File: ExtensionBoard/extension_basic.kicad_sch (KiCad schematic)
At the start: 11 parts, among them U1 KH-2.54FH-1X15P-H8.5, U1 Unidirectional 5.5V 6V SOT-14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, U2 C193852, U2 PM2.54-2*15, U3 KH-2.54PH180-3X15P-L11.5

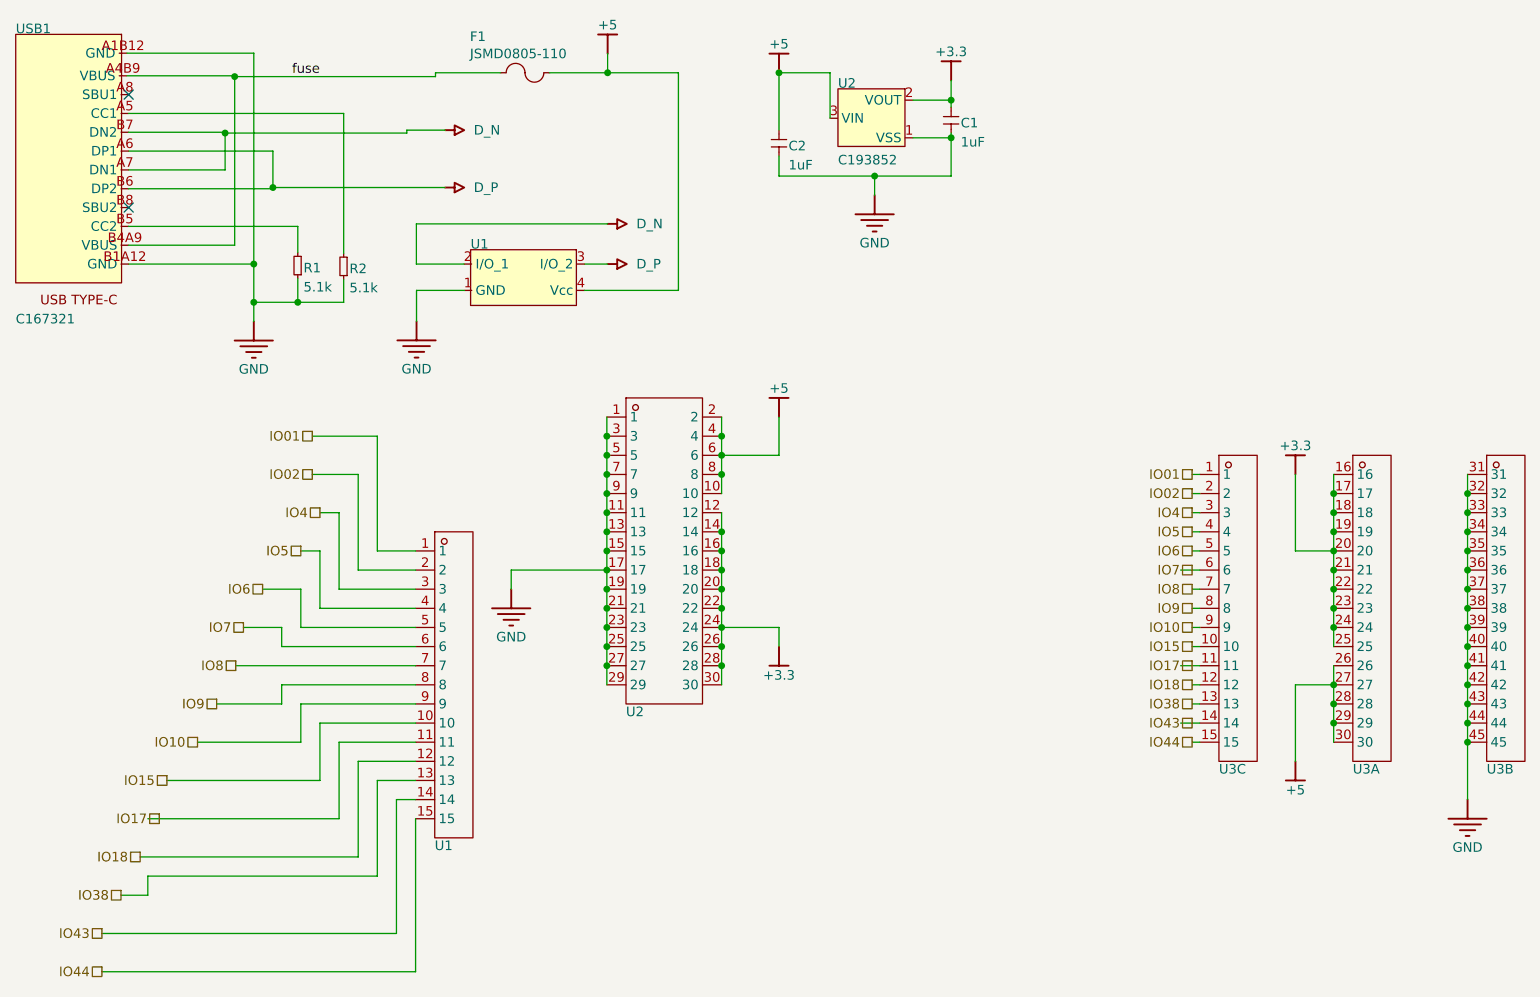
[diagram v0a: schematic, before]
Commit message: extension board imported
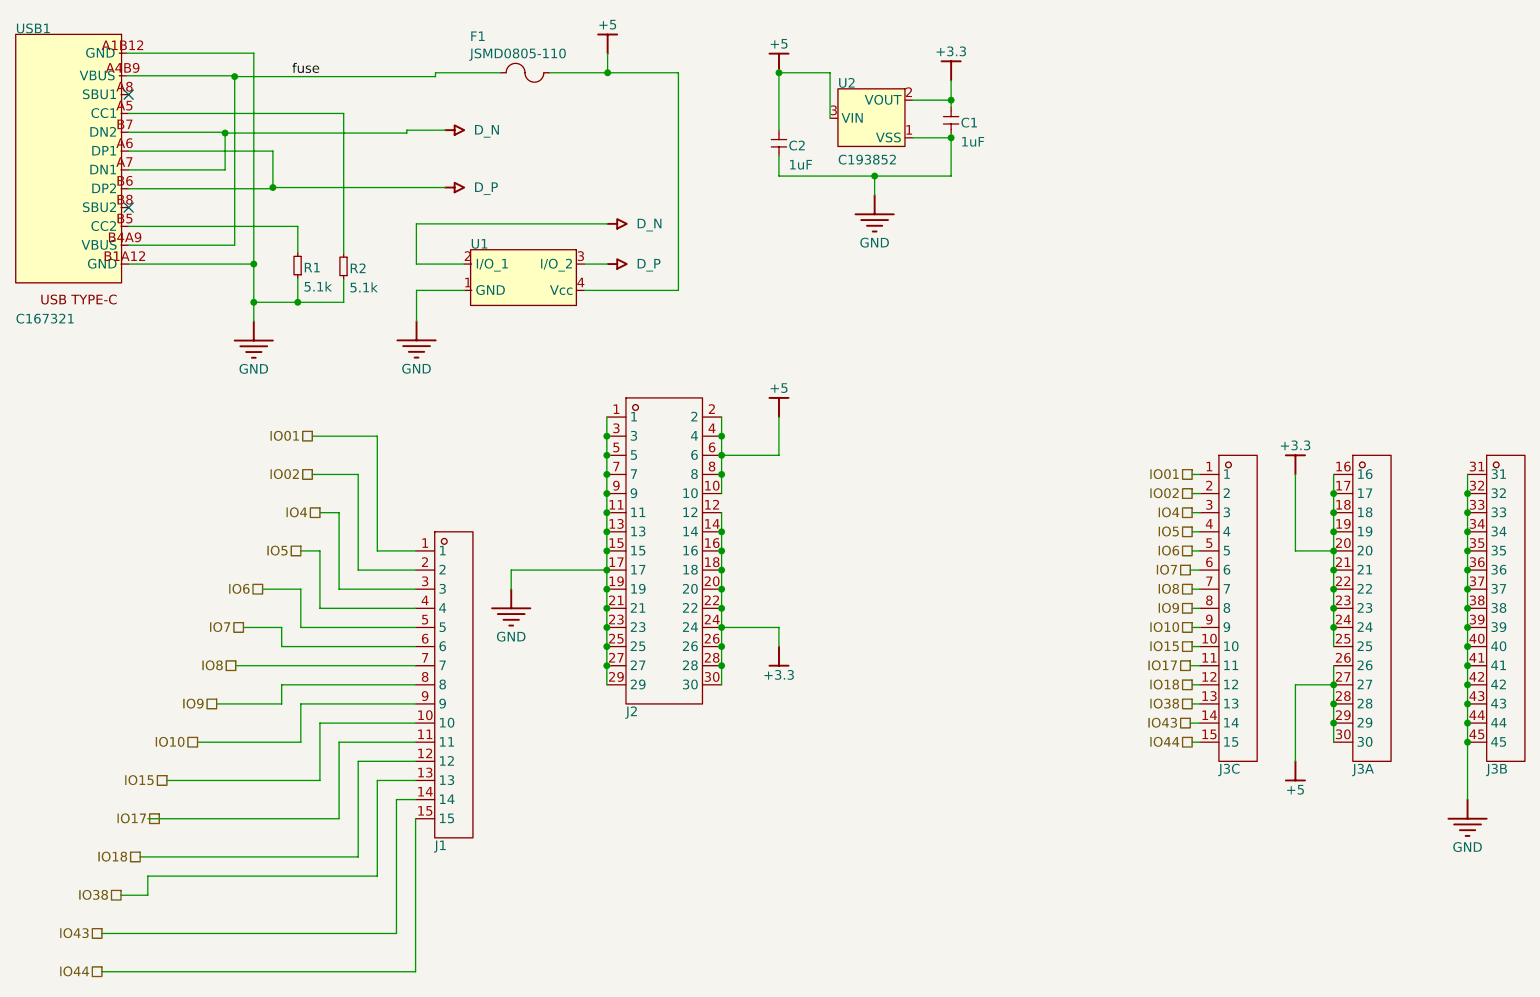
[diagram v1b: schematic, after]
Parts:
- removed U1: KH-2.54FH-1X15P-H8.5, HDR-TH_15P-P2.54-V-F, symbol KH-2.54FH-1X15P-H8.51_KH-2.54FH-1X15P-H8.5:root_0_KH-2.54FH-1X15P-H8.5_KH-2.54F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
- removed U2: PM2.54-2*15, HDR-TH_30P-P2.54-V-F-R2-C15-S2.54, symbol PM2.54-2_151_PM2.54-2_15:root_0_PM2.54-2*15_PM2.54-2_151_PM2.54-2_15.SCHLIB
- removed U3: KH-2.54PH180-3X15P-L11.5, HDR-TH_15P-P2.54-V-M-R3-C15-S2.54, symbol KH-2.54PH180-3X15P-L11.51_KH-2.54PH180-3X15P-L11.5:root_0_KH-2.54PH180-3X15P-L1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
- added J1: KH-2.54FH-1X15P-H8.5, FableFootPrintLibrary:HDR-TH_15P-P2.54-V-F, symbol KH-2.54FH-1X15P-H8.51_KH-2.54FH-1X15P-H8.5:root_0_KH-2.54FH-1X15P-H8.5_KH-2.54F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
- added J2: PM2.54-2*15, FableFootPrintLibrary:HDR-TH_30P-P2.54-V-F-R2-C15-S2.54, symbol PM2.54-2_151_PM2.54-2_15:root_0_PM2.54-2*15_PM2.54-2_151_PM2.54-2_15.SCHLIB
- added J3: KH-2.54PH180-3X15P-L11.5, FableFootPrintLibrary:HDR-TH_15P-P2.54-V-M-R3-C15-S2.54, symbol KH-2.54PH180-3X15P-L11.51_KH-2.54PH180-3X15P-L11.5:root_0_KH-2.54PH180-3X15P-L1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
- C1, C2: footprint 0402C -> FableFootPrintLibrary:0402C; SUPPLIER (none) -> LCSC; SUPPLIER PART (none) -> C107372
- F1: footprint 0805 -> FableFootPrintLibrary:0805; SUPPLIER (none) -> LCSC; SUPPLIER PART (none) -> C692712
- R1, R2: footprint FableFootPrintLibrary.PcbLib:0402R -> FableFootPrintLibrary:0402R; SUPPLIER (none) -> LCSC; SUPPLIER PART (none) -> C258132
- U1: footprint SOT143B -> FableFootPrintLibrary:SOT143B; SUPPLIER (none) -> LCSC; SUPPLIER PART (none) -> C12333
- U2: footprint SOT-23 -> FableFootPrintLibrary:SOT-23; SUPPLIER (none) -> LCSC; SUPPLIER PART (none) -> C193852
- USB1: footprint C167321 -> FableFootPrintLibrary:C167321; SUPPLIER (none) -> LCSC; SUPPLIER PART (none) -> C167321
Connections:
- net +3.3: now also J2.12, J2.14, J2.16, J2.18, J2.20, J2.22, J2.24, J2.26, J2.28, J2.30, J3.16, J3.17, J3.18, J3.19, J3.20, J3.21, J3.22, J3.23, J3.24, J3.25
- net +5: now also J2.10, J2.2, J2.4, J2.6, J2.8, J3.26, J3.27, J3.28, J3.29, J3.30
- net GND: now also J2.1, J2.11, J2.13, J2.15, J2.17, J2.19, J2.21, J2.23, J2.25, J2.27, J2.29, J2.3, J2.5, J2.7, J2.9, J3.31, J3.32, J3.33, J3.34, J3.35, J3.36, J3.37, J3.38, J3.39, J3.40, J3.41, J3.42, J3.43, J3.44, J3.45
- net IO01: now also J1.1, J3.1
- net IO02: now also J1.2, J3.2
- net IO10: now also J1.9, J3.9
- net IO15: now also J1.10, J3.10
- net IO17: now also J1.11, J3.11
- net IO18: now also J1.12, J3.12
- net IO38: now also J1.13, J3.13
- net IO4: now also J1.3, J3.3
- net IO43: now also J1.14, J3.14
- net IO44: now also J1.15, J3.15
- net IO5: now also J1.4, J3.4
- net IO6: now also J1.5, J3.5
- net IO7: now also J1.6, J3.6
- net IO8: now also J1.7, J3.7
- net IO9: now also J1.8, J3.8
